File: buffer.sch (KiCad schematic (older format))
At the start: 11 parts, among them U1 LFE5U-12F-8BG256C, U10 74LVC245, U11 74LVC245, U12 TXS0104E, U3 74LVC245, U4 74LVC245, U5 74LVC245, U6 74LVC245, U7 74LVC245, U8 74LVC245, U9 74LVC245

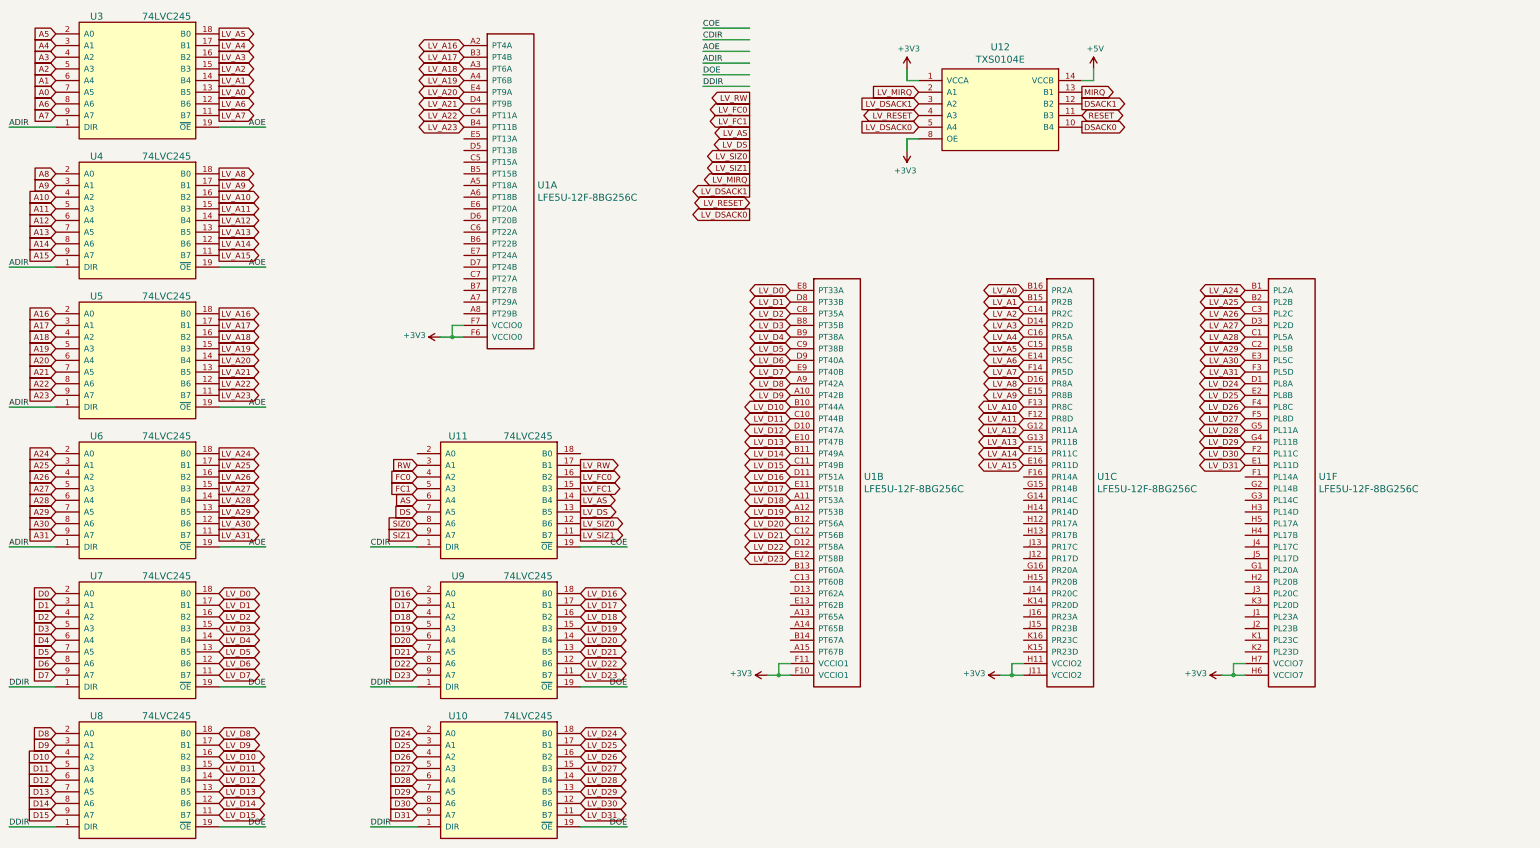
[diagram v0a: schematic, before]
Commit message: fanout finished and starting work on level translators
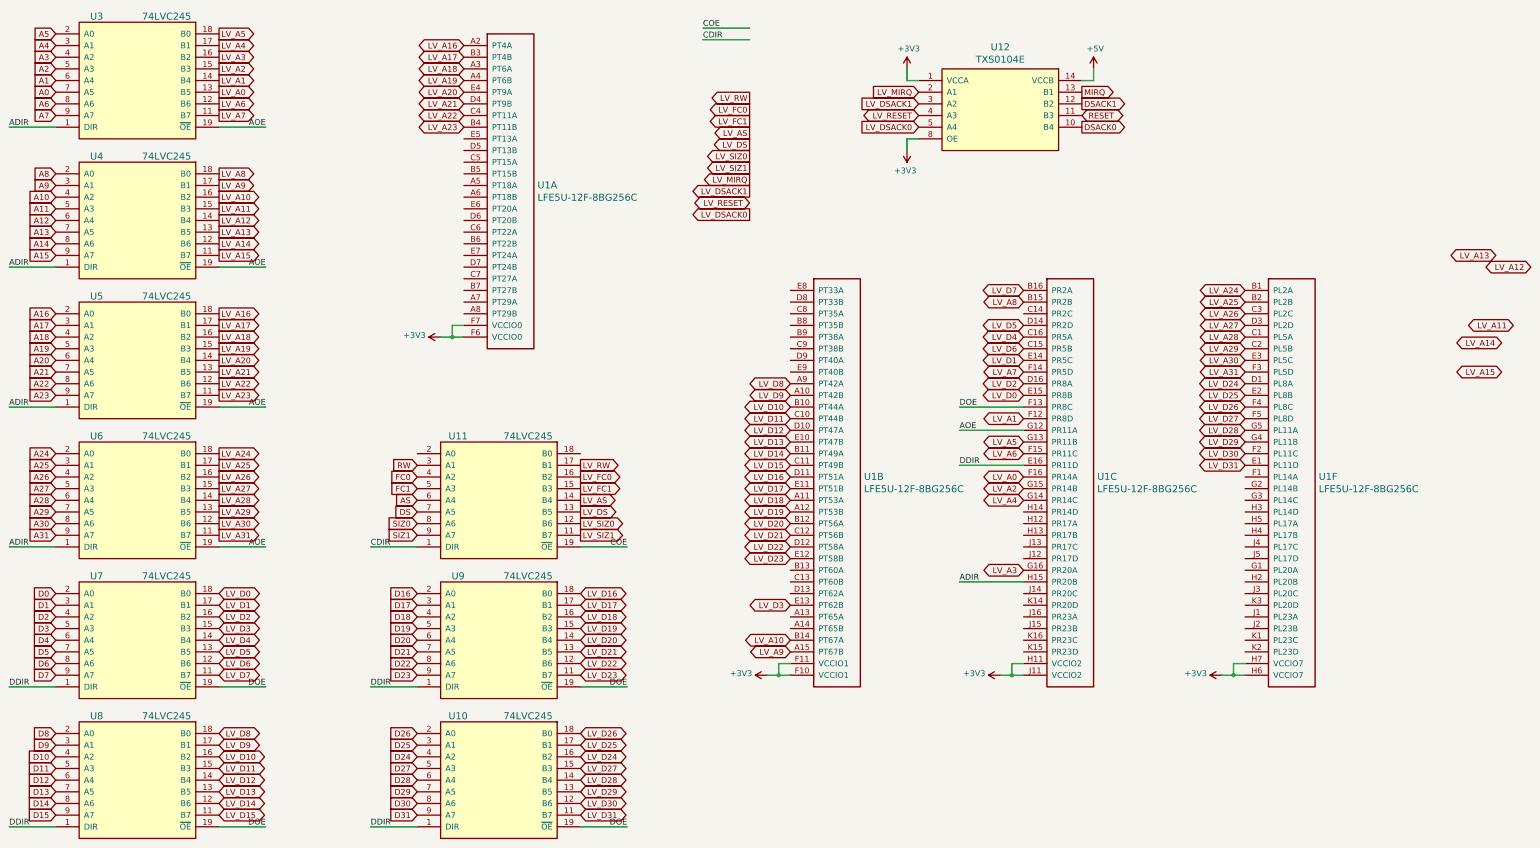
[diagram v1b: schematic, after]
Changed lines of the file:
@@
 Text GLabel 4300 6200 0    50   Input ~ 0
 D23
-Text GLabel 4300 6700 0    50   Input ~ 0
+Text GLabel 4300 6900 0    50   Input ~ 0
 D24
 Text GLabel 4300 6800 0    50   Input ~ 0
 D25
-Text GLabel 4300 6900 0    50   Input ~ 0
+Text GLabel 4300 6700 0    50   Input ~ 0
 D26
 Text GLabel 4300 7000 0    50   Input ~ 0
@@
 Text GLabel 5700 6200 2    50   BiDi ~ 0
 LV_D23
-Text GLabel 5700 6700 2    50   BiDi ~ 0
+Text GLabel 5700 6900 2    50   BiDi ~ 0
 LV_D24
 Text GLabel 5700 6800 2    50   BiDi ~ 0
 LV_D25
-Text GLabel 5700 6900 2    50   BiDi ~ 0
+Text GLabel 5700 6700 2    50   BiDi ~ 0
 LV_D26
 Text GLabel 5700 7000 2    50   BiDi ~ 0
@@
 Wire Wire Line
 	8500 1600 8500 1700
-Text GLabel 7500 2900 0    50   BiDi ~ 0
+Text GLabel 9500 3800 0    50   BiDi ~ 0
 LV_D0
-Text GLabel 7500 3000 0    50   BiDi ~ 0
+Text GLabel 9500 3500 0    50   BiDi ~ 0
 LV_D1
-Text GLabel 7500 3100 0    50   BiDi ~ 0
+Text GLabel 9500 3700 0    50   BiDi ~ 0
 LV_D2
-Text GLabel 7500 3200 0    50   BiDi ~ 0
+Text GLabel 7500 5600 0    50   BiDi ~ 0
 LV_D3
-Text GLabel 7500 3300 0    50   BiDi ~ 0
+Text GLabel 9500 3300 0    50   BiDi ~ 0
 LV_D4
-Text GLabel 7500 3400 0    50   BiDi ~ 0
+Text GLabel 9500 3200 0    50   BiDi ~ 0
 LV_D5
-Text GLabel 7500 3500 0    50   BiDi ~ 0
+Text GLabel 9500 3400 0    50   BiDi ~ 0
 LV_D6
-Text GLabel 7500 3600 0    50   BiDi ~ 0
+Text GLabel 9500 2900 0    50   BiDi ~ 0
 LV_D7
 Text GLabel 7500 3700 0    50   BiDi ~ 0
@@
 Text GLabel 11400 4400 0    50   BiDi ~ 0
 LV_D31
-Text GLabel 9500 2900 0    50   BiDi ~ 0
+Text GLabel 9500 4500 0    50   BiDi ~ 0
 LV_A0
-Text GLabel 9500 3000 0    50   BiDi ~ 0
+Text GLabel 9500 4000 0    50   BiDi ~ 0
 LV_A1
-Text GLabel 9500 3100 0    50   BiDi ~ 0
+Text GLabel 9500 4600 0    50   BiDi ~ 0
 LV_A2
-Text GLabel 9500 3200 0    50   BiDi ~ 0
+Text GLabel 9500 5300 0    50   BiDi ~ 0
 LV_A3
-Text GLabel 9500 3300 0    50   BiDi ~ 0
+Text GLabel 9500 4700 0    50   BiDi ~ 0
 LV_A4
-Text GLabel 9500 3400 0    50   BiDi ~ 0
+Text GLabel 9500 4200 0    50   BiDi ~ 0
 LV_A5
-Text GLabel 9500 3500 0    50   BiDi ~ 0
+Text GLabel 9500 4300 0    50   BiDi ~ 0
 LV_A6
 Text GLabel 9500 3600 0    50   BiDi ~ 0
 LV_A7
-Text GLabel 9500 3700 0    50   BiDi ~ 0
+Text GLabel 9500 3000 0    50   BiDi ~ 0
 LV_A8
-Text GLabel 9500 3800 0    50   BiDi ~ 0
+Text GLabel 7500 6000 0    50   BiDi ~ 0
 LV_A9
-Text GLabel 9500 3900 0    50   BiDi ~ 0
+Text GLabel 7500 5900 0    50   BiDi ~ 0
 LV_A10
-Text GLabel 9500 4000 0    50   BiDi ~ 0
+Text GLabel 13700 3200 0    50   BiDi ~ 0
 LV_A11
-Text GLabel 9500 4100 0    50   BiDi ~ 0
+Text GLabel 13850 2700 0    50   BiDi ~ 0
 LV_A12
-Text GLabel 9500 4200 0    50   BiDi ~ 0
+Text GLabel 13550 2600 0    50   BiDi ~ 0
 LV_A13
-Text GLabel 9500 4300 0    50   BiDi ~ 0
+Text GLabel 13600 3350 0    50   BiDi ~ 0
 LV_A14
-Text GLabel 9500 4400 0    50   BiDi ~ 0
+Text GLabel 13600 3600 0    50   BiDi ~ 0
 LV_A15
 Text GLabel 4700 800  0    50   BiDi ~ 0
@@
 LV_SIZ1
 Wire Wire Line
-	6750 850  7150 850
-Text Label 6750 850  0    50   ~ 0
+	8950 4100 9500 4100
+Text Label 8950 4100 0    50   ~ 0
 AOE
 Wire Wire Line
@@
 COE
 Wire Wire Line
-	6750 950  7150 950
-Text Label 6750 950  0    50   ~ 0
+	8950 5400 9500 5400
+Text Label 8950 5400 0    50   ~ 0
 ADIR
 Wire Wire Line
-	6750 1050 7150 1050
-Text Label 6750 1050 0    50   ~ 0
+	8950 3900 9500 3900
+Text Label 8950 3900 0    50   ~ 0
 DOE
 Wire Wire Line
-	6750 1150 7150 1150
-Text Label 6750 1150 0    50   ~ 0
+	8950 4400 9500 4400
+Text Label 8950 4400 0    50   ~ 0
 DDIR
 Wire Wire Line

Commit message: level translators done
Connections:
- no-connect marks 0 -> 5
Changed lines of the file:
@@
 Text Label 6100 5100 2    50   ~ 0
 COE
+Text GLabel 4300 5000 0    50   Input ~ 0
+RW
 Text GLabel 4300 4400 0    50   Input ~ 0
-RW
-Text GLabel 4300 5000 0    50   Input ~ 0
 SIZ1
-Text GLabel 4300 4900 0    50   Input ~ 0
+Text GLabel 4300 4500 0    50   Input ~ 0
 SIZ0
-Text GLabel 4300 4800 0    50   Input ~ 0
+Text GLabel 4300 4600 0    50   Input ~ 0
 DS
 Text GLabel 4300 4700 0    50   Input ~ 0
 AS
-Text GLabel 4300 4600 0    50   Input ~ 0
+Text GLabel 4300 4800 0    50   Input ~ 0
 FC1
-Text GLabel 4300 4500 0    50   Input ~ 0
+Text GLabel 4300 4900 0    50   Input ~ 0
 FC0
 Text GLabel 2600 1200 2    50   Output ~ 0
@@
 Text GLabel 5700 7400 2    50   BiDi ~ 0
 LV_D31
-Text GLabel 5700 4400 2    50   Output ~ 0
+Text GLabel 5700 5000 2    50   Output ~ 0
 LV_RW
-Text GLabel 5700 4500 2    50   Output ~ 0
+Text GLabel 5700 4900 2    50   Output ~ 0
 LV_FC0
-Text GLabel 5700 4600 2    50   Output ~ 0
+Text GLabel 5700 4800 2    50   Output ~ 0
 LV_FC1
 Text GLabel 5700 4700 2    50   Output ~ 0
 LV_AS
-Text GLabel 5700 4800 2    50   Output ~ 0
+Text GLabel 5700 4600 2    50   Output ~ 0
 LV_DS
-Text GLabel 5700 4900 2    50   Output ~ 0
+Text GLabel 5700 4500 2    50   Output ~ 0
 LV_SIZ0
-Text GLabel 5700 5000 2    50   Output ~ 0
+Text GLabel 5700 4400 2    50   Output ~ 0
 LV_SIZ1
 Wire Wire Line
@@
 Wire Wire Line
 	8500 1100 8500 1000
-Text GLabel 10000 1300 2    50   Output ~ 0
+Text GLabel 10000 1400 2    50   Output ~ 0
 DSACK1
+Text GLabel 10000 1200 2    50   Output ~ 0
+DSACK0
+Text GLabel 10000 1300 2    50   BiDi ~ 0
+RESET
 Text GLabel 10000 1500 2    50   Output ~ 0
-DSACK0
-Text GLabel 10000 1400 2    50   BiDi ~ 0
-RESET
-Text GLabel 10000 1200 2    50   Output ~ 0
 MIRQ
-Text GLabel 8600 1300 0    50   Input ~ 0
+Text GLabel 8600 1400 0    50   Input ~ 0
 LV_DSACK1
+Text GLabel 8600 1200 0    50   Input ~ 0
+LV_DSACK0
+Text GLabel 8600 1300 0    50   BiDi ~ 0
+LV_RESET
 Text GLabel 8600 1500 0    50   Input ~ 0
-LV_DSACK0
-Text GLabel 8600 1400 0    50   BiDi ~ 0
-LV_RESET
-Text GLabel 8600 1200 0    50   Input ~ 0
 LV_MIRQ
 $Comp
@@
 Text GLabel 9500 2900 0    50   BiDi ~ 0
 LV_D7
+Text GLabel 7500 5100 0    50   BiDi ~ 0
+LV_D8
+Text GLabel 7500 5700 0    50   BiDi ~ 0
+LV_D9
+Text GLabel 7500 5000 0    50   BiDi ~ 0
+LV_D10
+Text GLabel 7500 4900 0    50   BiDi ~ 0
+LV_D11
+Text GLabel 7500 4500 0    50   BiDi ~ 0
+LV_D12
+Text GLabel 7500 4800 0    50   BiDi ~ 0
+LV_D13
+Text GLabel 7500 4400 0    50   BiDi ~ 0
+LV_D14
+Text GLabel 7500 4300 0    50   BiDi ~ 0
+LV_D15
+Text GLabel 7500 2900 0    50   BiDi ~ 0
+LV_D16
 Text GLabel 7500 3700 0    50   BiDi ~ 0
-LV_D8
-Text GLabel 7500 3800 0    50   BiDi ~ 0
-LV_D9
-Text GLabel 7500 3900 0    50   BiDi ~ 0
-LV_D10
-Text GLabel 7500 4000 0    50   BiDi ~ 0
-LV_D11
-Text GLabel 7500 4100 0    50   BiDi ~ 0
-LV_D12
-Text GLabel 7500 4200 0    50   BiDi ~ 0
-LV_D13
-Text GLabel 7500 4300 0    50   BiDi ~ 0
-LV_D14
-Text GLabel 7500 4400 0    50   BiDi ~ 0
-LV_D15
-Text GLabel 7500 4500 0    50   BiDi ~ 0
-LV_D16
-Text GLabel 7500 4600 0    50   BiDi ~ 0
 LV_D17
-Text GLabel 7500 4700 0    50   BiDi ~ 0
+Text GLabel 7500 3000 0    50   BiDi ~ 0
 LV_D18
-Text GLabel 7500 4800 0    50   BiDi ~ 0
+Text GLabel 7500 3100 0    50   BiDi ~ 0
 LV_D19
-Text GLabel 7500 4900 0    50   BiDi ~ 0
+Text GLabel 4700 2600 0    50   BiDi ~ 0
 LV_D20
-Text GLabel 7500 5000 0    50   BiDi ~ 0
+Text GLabel 4700 3100 0    50   BiDi ~ 0
 LV_D21
-Text GLabel 7500 5100 0    50   BiDi ~ 0
+Text GLabel 4700 2800 0    50   BiDi ~ 0
 LV_D22
-Text GLabel 7500 5200 0    50   BiDi ~ 0
+Text GLabel 7500 3200 0    50   BiDi ~ 0
 LV_D23
-Text GLabel 11400 3700 0    50   BiDi ~ 0
+Text GLabel 4700 1400 0    50   BiDi ~ 0
 LV_D24
-Text GLabel 11400 3800 0    50   BiDi ~ 0
+Text GLabel 4700 2000 0    50   BiDi ~ 0
 LV_D25
-Text GLabel 11400 3900 0    50   BiDi ~ 0
+Text GLabel 4700 1700 0    50   BiDi ~ 0
 LV_D26
-Text GLabel 11400 4000 0    50   BiDi ~ 0
+Text GLabel 4700 1900 0    50   BiDi ~ 0
 LV_D27
-Text GLabel 11400 4100 0    50   BiDi ~ 0
+Text GLabel 4700 1300 0    50   BiDi ~ 0
 LV_D28
-Text GLabel 11400 4200 0    50   BiDi ~ 0
+Text GLabel 4700 1100 0    50   BiDi ~ 0
 LV_D29
-Text GLabel 11400 4300 0    50   BiDi ~ 0
+Text GLabel 4700 1500 0    50   BiDi ~ 0
 LV_D30
-Text GLabel 11400 4400 0    50   BiDi ~ 0
+Text GLabel 4700 1000 0    50   BiDi ~ 0
 LV_D31
 Text GLabel 9500 4500 0    50   BiDi ~ 0
@@
 Text GLabel 7500 5900 0    50   BiDi ~ 0
 LV_A10
-Text GLabel 13700 3200 0    50   BiDi ~ 0
+Text GLabel 9500 3100 0    50   BiDi ~ 0
 LV_A11
-Text GLabel 13850 2700 0    50   BiDi ~ 0
+Text GLabel 7500 5800 0    50   BiDi ~ 0
 LV_A12
-Text GLabel 13550 2600 0    50   BiDi ~ 0
+Text GLabel 7500 5500 0    50   BiDi ~ 0
 LV_A13
-Text GLabel 13600 3350 0    50   BiDi ~ 0
+Text GLabel 7500 5300 0    50   BiDi ~ 0
 LV_A14
-Text GLabel 13600 3600 0    50   BiDi ~ 0
+Text GLabel 7500 5400 0    50   BiDi ~ 0
 LV_A15
-Text GLabel 4700 800  0    50   BiDi ~ 0
+Text GLabel 7500 4100 0    50   BiDi ~ 0
 LV_A16
-Text GLabel 4700 900  0    50   BiDi ~ 0
+Text GLabel 7500 4700 0    50   BiDi ~ 0
 LV_A17
-Text GLabel 4700 1000 0    50   BiDi ~ 0
+Text GLabel 7500 4000 0    50   BiDi ~ 0
 LV_A18
-Text GLabel 4700 1100 0    50   BiDi ~ 0
+Text GLabel 7500 3900 0    50   BiDi ~ 0
 LV_A19
-Text GLabel 4700 1200 0    50   BiDi ~ 0
+Text GLabel 7500 3500 0    50   BiDi ~ 0
 LV_A20
-Text GLabel 4700 1300 0    50   BiDi ~ 0
+Text GLabel 7500 3800 0    50   BiDi ~ 0
 LV_A21
-Text GLabel 4700 1400 0    50   BiDi ~ 0
+Text GLabel 7500 3400 0    50   BiDi ~ 0
 LV_A22
-Text GLabel 4700 1500 0    50   BiDi ~ 0
+Text GLabel 7500 3300 0    50   BiDi ~ 0
 LV_A23
-Text GLabel 11400 2900 0    50   BiDi ~ 0
+Text GLabel 4700 2700 0    50   BiDi ~ 0
 LV_A24
-Text GLabel 11400 3000 0    50   BiDi ~ 0
+Text GLabel 4700 3000 0    50   BiDi ~ 0
 LV_A25
-Text GLabel 11400 3100 0    50   BiDi ~ 0
+Text GLabel 4700 2400 0    50   BiDi ~ 0
 LV_A26
-Text GLabel 11400 3200 0    50   BiDi ~ 0
+Text GLabel 4700 2900 0    50   BiDi ~ 0
 LV_A27
-Text GLabel 11400 3300 0    50   BiDi ~ 0
+Text GLabel 4700 2300 0    50   BiDi ~ 0
 LV_A28
-Text GLabel 11400 3400 0    50   BiDi ~ 0
+Text GLabel 4700 2100 0    50   BiDi ~ 0
 LV_A29
-Text GLabel 11400 3500 0    50   BiDi ~ 0
+Text GLabel 4700 1800 0    50   BiDi ~ 0
 LV_A30
-Text GLabel 11400 3600 0    50   BiDi ~ 0
+Text GLabel 4700 2500 0    50   BiDi ~ 0
 LV_A31
-Text GLabel 7150 2050 0    50   Output ~ 0
-LV_DSACK1
-Text GLabel 7150 2250 0    50   Output ~ 0
-LV_DSACK0
-Text GLabel 7150 2150 0    50   BiDi ~ 0
-LV_RESET
-Text GLabel 7150 1950 0    50   Output ~ 0
-LV_MIRQ
-Text GLabel 7150 1250 0    50   Output ~ 0
-LV_RW
-Text GLabel 7150 1350 0    50   Output ~ 0
-LV_FC0
-Text GLabel 7150 1450 0    50   Output ~ 0
-LV_FC1
-Text GLabel 7150 1550 0    50   Output ~ 0
-LV_AS
-Text GLabel 7150 1650 0    50   Output ~ 0
-LV_DS
-Text GLabel 7150 1750 0    50   Output ~ 0
-LV_SIZ0
-Text GLabel 7150 1850 0    50   Output ~ 0
-LV_SIZ1
 Wire Wire Line
 	8950 4100 9500 4100
 Text Label 8950 4100 0    50   ~ 0
 AOE
-Wire Wire Line
-	6750 750  7150 750
-Text Label 6750 750  0    50   ~ 0
-CDIR
-Wire Wire Line
-	6750 650  7150 650
-Text Label 6750 650  0    50   ~ 0
-COE
 Wire Wire Line
 	8950 5400 9500 5400
@@
 	0    -1   -1   0
 $EndComp
+Text GLabel 4700 1600 0    50   Output ~ 0
+LV_DSACK1
+Text GLabel 4700 1200 0    50   Output ~ 0
+LV_DSACK0
+Text GLabel 4700 800  0    50   BiDi ~ 0
+LV_RESET
+Text GLabel 4700 900  0    50   Output ~ 0
+LV_MIRQ
+Text GLabel 9500 4800 0    50   Output ~ 0
+LV_RW
+Text GLabel 9500 5000 0    50   Output ~ 0
+LV_FC0
+Text GLabel 9500 5700 0    50   Output ~ 0
+LV_FC1
+Text GLabel 9500 5100 0    50   Output ~ 0
+LV_AS
+Text GLabel 9500 5800 0    50   Output ~ 0
+LV_DS
+Text GLabel 9500 5500 0    50   Output ~ 0
+LV_SIZ0
+Text GLabel 9500 5900 0    50   Output ~ 0
+LV_SIZ1
+Wire Wire Line
+	8950 6000 9500 6000
+Text Label 8950 6000 0    50   ~ 0
+COE
+Wire Wire Line
+	8950 5600 9500 5600
+Text Label 8950 5600 0    50   ~ 0
+CDIR
+NoConn ~ 4700 2200
+NoConn ~ 7500 5200
+NoConn ~ 7500 4600
+NoConn ~ 7500 4200
+NoConn ~ 7500 3600
 $EndSCHEMATC
